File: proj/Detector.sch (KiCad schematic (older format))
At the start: 13 parts, among them U11 AD8310ARMZ

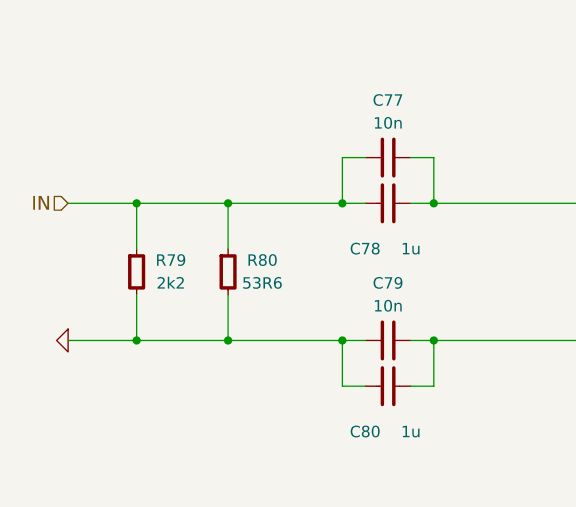
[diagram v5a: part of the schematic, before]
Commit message: Clean up resistor BOM
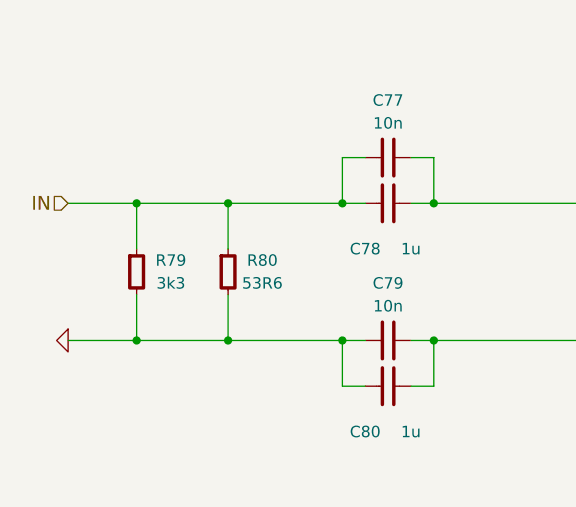
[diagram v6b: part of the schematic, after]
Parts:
- R79: value 2k2 -> 3k3; BOM RES SMD 2.2k 1% [0402] -> RES SMD 3.3k 5% [0402]
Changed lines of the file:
@@
 $Descr USLegal 14000 8500
 encoding utf-8
-Sheet 12 13
+Sheet 10 13
 Title "Logarithmic Detector"
 Date "2015-02-28"
@@
 P 4000 3750
 F 0 "R79" H 4150 3800 50  0000 C CNN
-F 1 "2k2" H 4150 3700 50  0000 C CNN
+F 1 "3k3" H 4150 3700 50  0000 C CNN
 F 2 "IPC7351-Nominal:RESC1005X40" H 4000 3750 50  0001 C CNN
 F 3 "" H 4000 3800 60  0000 C CNN
 F 4 "Value" H 4000 3750 60  0001 C CNN "Manuf"
-F 5 "RES SMD 2.2k 1% [0402]" H 4750 4300 60  0001 C CNN "BOM"
+F 5 "RES SMD 3.3k 5% [0402]" H 4750 4300 60  0001 C CNN "BOM"
 	1    4000 3750
 	1    0    0    -1
@@
 	9500 3650 9100 3650
 $Comp
-L GND #PWR0192
+L GND #PWR0190
 U 1 1 54F233FD
 P 9800 3650
-F 0 "#PWR0192" H 9800 3650 30  0001 C CNN
+F 0 "#PWR0190" H 9800 3650 30  0001 C CNN
 F 1 "GND" H 9800 3580 30  0001 C CNN
 F 2 "" H 9800 3650 60  0000 C CNN
@@
 	9600 4250 9100 4250
 $Comp
-L GND #PWR0193
+L GND #PWR0191
 U 1 1 54F23584
 P 9600 4650
-F 0 "#PWR0193" H 9600 4650 30  0001 C CNN
+F 0 "#PWR0191" H 9600 4650 30  0001 C CNN
 F 1 "GND" H 9600 4580 30  0001 C CNN
 F 2 "" H 9600 4650 60  0000 C CNN
@@
 	9600 4650 9600 4550
 $Comp
-L GND #PWR0194
+L GND #PWR0192
 U 1 1 54F235D2
 P 9200 4650
-F 0 "#PWR0194" H 9200 4650 30  0001 C CNN
+F 0 "#PWR0192" H 9200 4650 30  0001 C CNN
 F 1 "GND" H 9200 4580 30  0001 C CNN
 F 2 "" H 9200 4650 60  0000 C CNN
@@
 	8500 2350 8500 2450
 $Comp
-L GND #PWR0195
+L GND #PWR0193
 U 1 1 54F23A44
 P 8500 2700
-F 0 "#PWR0195" H 8500 2700 30  0001 C CNN
+F 0 "#PWR0193" H 8500 2700 30  0001 C CNN
 F 1 "GND" H 8500 2630 30  0001 C CNN
 F 2 "" H 8500 2700 60  0000 C CNN
@@
 $EndComp
 $Comp
-L GND #PWR0196
+L GND #PWR0194
 U 1 1 54F23F3E
 P 7900 2700
-F 0 "#PWR0196" H 7900 2700 30  0001 C CNN
+F 0 "#PWR0194" H 7900 2700 30  0001 C CNN
 F 1 "GND" H 7900 2630 30  0001 C CNN
 F 2 "" H 7900 2700 60  0000 C CNN
@@
 Connection ~ 7900 2350
 $Comp
-L GND #PWR0197
+L GND #PWR0195
 U 1 1 54F24135
 P 7400 2700
-F 0 "#PWR0197" H 7400 2700 30  0001 C CNN
+F 0 "#PWR0195" H 7400 2700 30  0001 C CNN
 F 1 "GND" H 7400 2630 30  0001 C CNN
 F 2 "" H 7400 2700 60  0000 C CNN
@@
 Connection ~ 6800 2350
 $Comp
-L +5 #PWR0198
+L +5 #PWR0196
 U 1 1 54F24371
 P 6800 1900
-F 0 "#PWR0198" H 6800 1950 30  0001 C CNN
+F 0 "#PWR0196" H 6800 1950 30  0001 C CNN
 F 1 "+5" H 6800 2000 50  0000 C CNN
 F 2 "" H 6800 1900 60  0000 C CNN
@@
 Connection ~ 4000 3450
 $Comp
-L GND #PWR0199
+L GND #PWR0197
 U 1 1 54F24ACA
 P 3700 4050
-F 0 "#PWR0199" H 3700 4050 30  0001 C CNN
+F 0 "#PWR0197" H 3700 4050 30  0001 C CNN
 F 1 "GND" H 3700 3980 30  0001 C CNN
 F 2 "" H 3700 4050 60  0000 C CNN

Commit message: Swap 0402 to 0603, add USB inrush protection
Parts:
- removed C77, C79, C81: 10n, IPC7351-Nominal:CAPC1005X55, symbol C-0402
- removed C82: 680n, IPC7351-Nominal:CAPC2012X70, symbol C-0805
- removed R79: 3k3, IPC7351-Nominal:RESC1005X40, symbol R-0402
- removed R80: 53R6, IPC7351-Nominal:RESC1005X40, symbol R-0402
- removed R81: 49R9, IPC7351-Nominal:RESC1005X40, symbol R-0402
- added C57, C58, C59: 10n, IPC7351-Nominal:CAPC1608X55, symbol C-0603
- added C60: 100n, IPC7351-Nominal:CAPC1608X55, symbol C-0603
- added R79: 3k3, IPC7351-Nominal:RESC1608X50, symbol R-0603
- added R80: 53R6, IPC7351-Nominal:RESC1608X50, symbol R-0603
- added R81: 49R9, IPC7351-Nominal:RESC1608X50, symbol R-0603
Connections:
- net +5: now also R81.1
- net 4V6_FILTERED: now also C59.1, C60.1, R81.2
- net GND: now also C58.2, C59.2, C60.2, R79.2, R80.2
- net IN: now also C57.2, R79.1, R80.1
- net at C80.1, U11.1 (IN-): now also C58.1
- net at C78.1, U11.8 (IN+): now also C57.1
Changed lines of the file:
@@
 	0    1    1    0
-$EndComp
-$Comp
-L C-0402 C77
-U 1 1 54F3B21C
-P 5100 3250
-F 0 "C77" V 5350 3250 50  0000 C CNN
-F 1 "10n" V 5250 3250 50  0000 C CNN
-F 2 "IPC7351-Nominal:CAPC1005X55" H 5100 3250 50  0001 C CNN
-F 3 "" H 5090 3225 60  0000 C CNN
-F 4 "Value" H 5100 3250 60  0001 C CNN "Manuf"
-F 5 "CAP MLCC 10n ≥X5R 25V 10% [0402]" H 5900 3800 60  0001 C CNN "BOM"
-	1    5100 3250
-	0    1    -1   0
-$EndComp
-$Comp
-L R-0402 R80
-U 1 1 54F3B598
-P 4400 3750
-F 0 "R80" H 4550 3800 50  0000 C CNN
-F 1 "53R6" H 4550 3700 50  0000 C CNN
-F 2 "IPC7351-Nominal:RESC1005X40" H 4400 3750 50  0001 C CNN
-F 3 "" H 4400 3800 60  0000 C CNN
-F 4 "Value" H 4400 3750 60  0001 C CNN "Manuf"
-F 5 "RES SMD 53.6 1% [0402]" H 5150 4300 60  0001 C CNN "BOM"
-	1    4400 3750
-	1    0    0    -1
-$EndComp
-$Comp
-L R-0402 R79
-U 1 1 54F3B632
-P 4000 3750
-F 0 "R79" H 4150 3800 50  0000 C CNN
-F 1 "3k3" H 4150 3700 50  0000 C CNN
-F 2 "IPC7351-Nominal:RESC1005X40" H 4000 3750 50  0001 C CNN
-F 3 "" H 4000 3800 60  0000 C CNN
-F 4 "Value" H 4000 3750 60  0001 C CNN "Manuf"
-F 5 "RES SMD 3.3k 5% [0402]" H 4750 4300 60  0001 C CNN "BOM"
-	1    4000 3750
-	1    0    0    -1
 $EndComp
 Wire Wire Line
@@
 	4400 3850 4400 4050
 Connection ~ 4400 4050
-$Comp
-L C-0402 C79
-U 1 1 54F3B741
-P 5100 4050
-F 0 "C79" V 5350 4050 50  0000 C CNN
-F 1 "10n" V 5250 4050 50  0000 C CNN
-F 2 "IPC7351-Nominal:CAPC1005X55" H 5100 4050 50  0001 C CNN
-F 3 "" H 5090 4025 60  0000 C CNN
-F 4 "Value" H 5100 4050 60  0001 C CNN "Manuf"
-F 5 "CAP MLCC 10n ≥X5R 25V 10% [0402]" H 5900 4600 60  0001 C CNN "BOM"
-	1    5100 4050
-	0    1    -1   0
-$EndComp
 $Comp
 L C-0805 C80
@@
 	9500 3650 9100 3650
 $Comp
-L GND #PWR0190
+L GND #PWR0183
 U 1 1 54F233FD
 P 9800 3650
-F 0 "#PWR0190" H 9800 3650 30  0001 C CNN
+F 0 "#PWR0183" H 9800 3650 30  0001 C CNN
 F 1 "GND" H 9800 3580 30  0001 C CNN
 F 2 "" H 9800 3650 60  0000 C CNN
@@
 	9600 4250 9100 4250
 $Comp
-L GND #PWR0191
+L GND #PWR0184
 U 1 1 54F23584
 P 9600 4650
-F 0 "#PWR0191" H 9600 4650 30  0001 C CNN
+F 0 "#PWR0184" H 9600 4650 30  0001 C CNN
 F 1 "GND" H 9600 4580 30  0001 C CNN
 F 2 "" H 9600 4650 60  0000 C CNN
@@
 	9600 4650 9600 4550
 $Comp
-L GND #PWR0192
+L GND #PWR0185
 U 1 1 54F235D2
 P 9200 4650
-F 0 "#PWR0192" H 9200 4650 30  0001 C CNN
+F 0 "#PWR0185" H 9200 4650 30  0001 C CNN
 F 1 "GND" H 9200 4580 30  0001 C CNN
 F 2 "" H 9200 4650 60  0000 C CNN
@@
 	8500 2350 8500 2450
 $Comp
-L GND #PWR0193
+L GND #PWR0186
 U 1 1 54F23A44
 P 8500 2700
-F 0 "#PWR0193" H 8500 2700 30  0001 C CNN
+F 0 "#PWR0186" H 8500 2700 30  0001 C CNN
 F 1 "GND" H 8500 2630 30  0001 C CNN
 F 2 "" H 8500 2700 60  0000 C CNN
@@
 	8500 2700 8500 2650
 $Comp
-L C-0805 C82
-U 1 1 54F23E0B
-P 7900 2550
-F 0 "C82" H 8150 2600 50  0000 C CNN
-F 1 "680n" H 8150 2500 50  0000 C CNN
-F 2 "IPC7351-Nominal:CAPC2012X70" H 7900 2550 50  0001 C CNN
-F 3 "" H 7890 2525 60  0000 C CNN
-F 4 "Value" H 7900 2550 60  0001 C CNN "Manuf"
-F 5 "CAP MLCC 680n ≥X5R 16V 20% [0805]" H 8700 3100 60  0001 C CNN "BOM"
-	1    7900 2550
-	1    0    0    -1
-$EndComp
-$Comp
-L GND #PWR0194
+L GND #PWR0187
 U 1 1 54F23F3E
 P 7900 2700
-F 0 "#PWR0194" H 7900 2700 30  0001 C CNN
+F 0 "#PWR0187" H 7900 2700 30  0001 C CNN
 F 1 "GND" H 7900 2630 30  0001 C CNN
 F 2 "" H 7900 2700 60  0000 C CNN
@@
 	7900 2350 7900 2450
 Connection ~ 8500 2350
-$Comp
-L C-0402 C81
-U 1 1 54F24012
-P 7400 2550
-F 0 "C81" H 7600 2500 50  0000 C CNN
-F 1 "10n" H 7600 2600 50  0000 C CNN
-F 2 "IPC7351-Nominal:CAPC1005X55" H 7400 2550 50  0001 C CNN
-F 3 "" H 7390 2525 60  0000 C CNN
-F 4 "Value" H 7400 2550 60  0001 C CNN "Manuf"
-F 5 "CAP MLCC 10n ≥X5R 25V 10% [0402]" H 8200 3100 60  0001 C CNN "BOM"
-	1    7400 2550
-	1    0    0    1
-$EndComp
 Wire Wire Line
 	7400 2350 7400 2450
 Connection ~ 7900 2350
 $Comp
-L GND #PWR0195
+L GND #PWR0188
 U 1 1 54F24135
 P 7400 2700
-F 0 "#PWR0195" H 7400 2700 30  0001 C CNN
+F 0 "#PWR0188" H 7400 2700 30  0001 C CNN
 F 1 "GND" H 7400 2630 30  0001 C CNN
 F 2 "" H 7400 2700 60  0000 C CNN
@@
 	6800 2150 6800 3500
 Connection ~ 7400 2350
-$Comp
-L R-0402 R81
-U 1 1 54F24260
-P 6800 2050
-F 0 "R81" H 6950 2100 50  0000 C CNN
-F 1 "49R9" H 6950 2000 50  0000 C CNN
-F 2 "IPC7351-Nominal:RESC1005X40" H 6800 2050 50  0001 C CNN
-F 3 "" H 6800 2100 60  0000 C CNN
-F 4 "Value" H 6800 2050 60  0001 C CNN "Manuf"
-F 5 "RES SMD 49.9 1% [0402]" H 7550 2600 60  0001 C CNN "BOM"
-	1    6800 2050
-	1    0    0    -1
-$EndComp
 Connection ~ 6800 2350
 $Comp
-L +5 #PWR0196
+L +5 #PWR0189
 U 1 1 54F24371
 P 6800 1900
-F 0 "#PWR0196" H 6800 1950 30  0001 C CNN
+F 0 "#PWR0189" H 6800 1950 30  0001 C CNN
 F 1 "+5" H 6800 2000 50  0000 C CNN
 F 2 "" H 6800 1900 60  0000 C CNN
@@
 Connection ~ 4000 3450
 $Comp
-L GND #PWR0197
+L GND #PWR0190
 U 1 1 54F24ACA
 P 3700 4050
-F 0 "#PWR0197" H 3700 4050 30  0001 C CNN
+F 0 "#PWR0190" H 3700 4050 30  0001 C CNN
 F 1 "GND" H 3700 3980 30  0001 C CNN
 F 2 "" H 3700 4050 60  0000 C CNN
@@
 $EndComp
 Connection ~ 4000 4050
+$Comp
+L C-0603 C57
+U 1 1 54FF63E3
+P 5100 3250
+F 0 "C57" V 5350 3250 50  0000 C CNN
+F 1 "10n" V 5250 3250 50  0000 C CNN
+F 2 "IPC7351-Nominal:CAPC1608X55" H 5100 3250 50  0001 C CNN
+F 3 "" H 5090 3225 60  0000 C CNN
+F 4 "Value" H 5100 3250 60  0001 C CNN "Manuf"
+F 5 "CAP MLCC 10n ≥X5R 50V 10% [0603]" H 5900 3800 60  0001 C CNN "BOM"
+	1    5100 3250
+	0    1    -1   0
+$EndComp
+$Comp
+L C-0603 C58
+U 1 1 54FF6499
+P 5100 4050
+F 0 "C58" V 5350 4050 50  0000 C CNN
+F 1 "10n" V 5250 4050 50  0000 C CNN
+F 2 "IPC7351-Nominal:CAPC1608X55" H 5100 4050 50  0001 C CNN
+F 3 "" H 5090 4025 60  0000 C CNN
+F 4 "Value" H 5100 4050 60  0001 C CNN "Manuf"
+F 5 "CAP MLCC 10n ≥X5R 50V 10% [0603]" H 5900 4600 60  0001 C CNN "BOM"
+	1    5100 4050
+	0    1    -1   0
+$EndComp
+$Comp
+L C-0603 C59
+U 1 1 54FF9496
+P 7400 2550
+F 0 "C59" H 7600 2600 50  0000 C CNN
+F 1 "10n" H 7600 2500 50  0000 C CNN
+F 2 "IPC7351-Nominal:CAPC1608X55" H 7400 2550 50  0001 C CNN
+F 3 "" H 7390 2525 60  0000 C CNN
+F 4 "Value" H 7400 2550 60  0001 C CNN "Manuf"
+F 5 "CAP MLCC 10n ≥X5R 50V 10% [0603]" H 8200 3100 60  0001 C CNN "BOM"
+	1    7400 2550
+	1    0    0    -1
+$EndComp
+$Comp
+L C-0603 C60
+U 1 1 54FFA4C7
+P 7900 2550
+F 0 "C60" H 8100 2600 50  0000 C CNN
+F 1 "100n" H 8100 2500 50  0000 C CNN
+F 2 "IPC7351-Nominal:CAPC1608X55" H 7900 2550 50  0001 C CNN
+F 3 "" H 7890 2525 60  0000 C CNN
+F 4 "Value" H 7900 2550 60  0001 C CNN "Manuf"
+F 5 "CAP MLCC 100n ≥X7R 16V 10% [0603]" H 8700 3100 60  0001 C CNN "BOM"
+	1    7900 2550
+	1    0    0    -1
+$EndComp
+$Comp
+L R-0603 R79
+U 1 1 55030E37
+P 4000 3750
+F 0 "R79" H 4150 3800 50  0000 C CNN
+F 1 "3k3" H 4150 3700 50  0000 C CNN
+F 2 "IPC7351-Nominal:RESC1608X50" H 4000 3750 50  0001 C CNN
+F 3 "" H 4000 3800 60  0000 C CNN
+F 4 "Value" H 4000 3750 60  0001 C CNN "Manuf"
+F 5 "RES SMD 3.3k 5% [0603]" H 4750 4300 60  0001 C CNN "BOM"
+	1    4000 3750
+	1    0    0    -1
+$EndComp
+$Comp
+L R-0603 R80
+U 1 1 55030F3F
+P 4400 3750
+F 0 "R80" H 4600 3800 50  0000 C CNN
+F 1 "53R6" H 4600 3700 50  0000 C CNN
+F 2 "IPC7351-Nominal:RESC1608X50" H 4400 3750 50  0001 C CNN
+F 3 "" H 4400 3800 60  0000 C CNN
+F 4 "Value" H 4400 3750 60  0001 C CNN "Manuf"
+F 5 "RES SMD 53.6 1% [0603]" H 5150 4300 60  0001 C CNN "BOM"
+	1    4400 3750
+	1    0    0    -1
+$EndComp
+$Comp
+L R-0603 R81
+U 1 1 55036177
+P 6800 2050
+F 0 "R81" H 6950 2100 50  0000 C CNN
+F 1 "49R9" H 6950 2000 50  0000 C CNN
+F 2 "IPC7351-Nominal:RESC1608X50" H 6800 2050 50  0001 C CNN
+F 3 "" H 6800 2100 60  0000 C CNN
+F 4 "Value" H 6800 2050 60  0001 C CNN "Manuf"
+F 5 "RES SMD 49R9 1% [0603]" H 7550 2600 60  0001 C CNN "BOM"
+	1    6800 2050
+	1    0    0    -1
+$EndComp
 $EndSCHEMATC
